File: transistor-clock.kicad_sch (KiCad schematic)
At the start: 41 parts, among them J1 Screw_Terminal_01x02, Q1 MMBT3904, Q2 MMBT3904, Q3 MMBT3904, Q4 DMP3099L, Q5 2N7002, Q6 MMBT3904, Q7 MMBT3904, Q8 MMBT3904, T1 Transformer_1P_SS

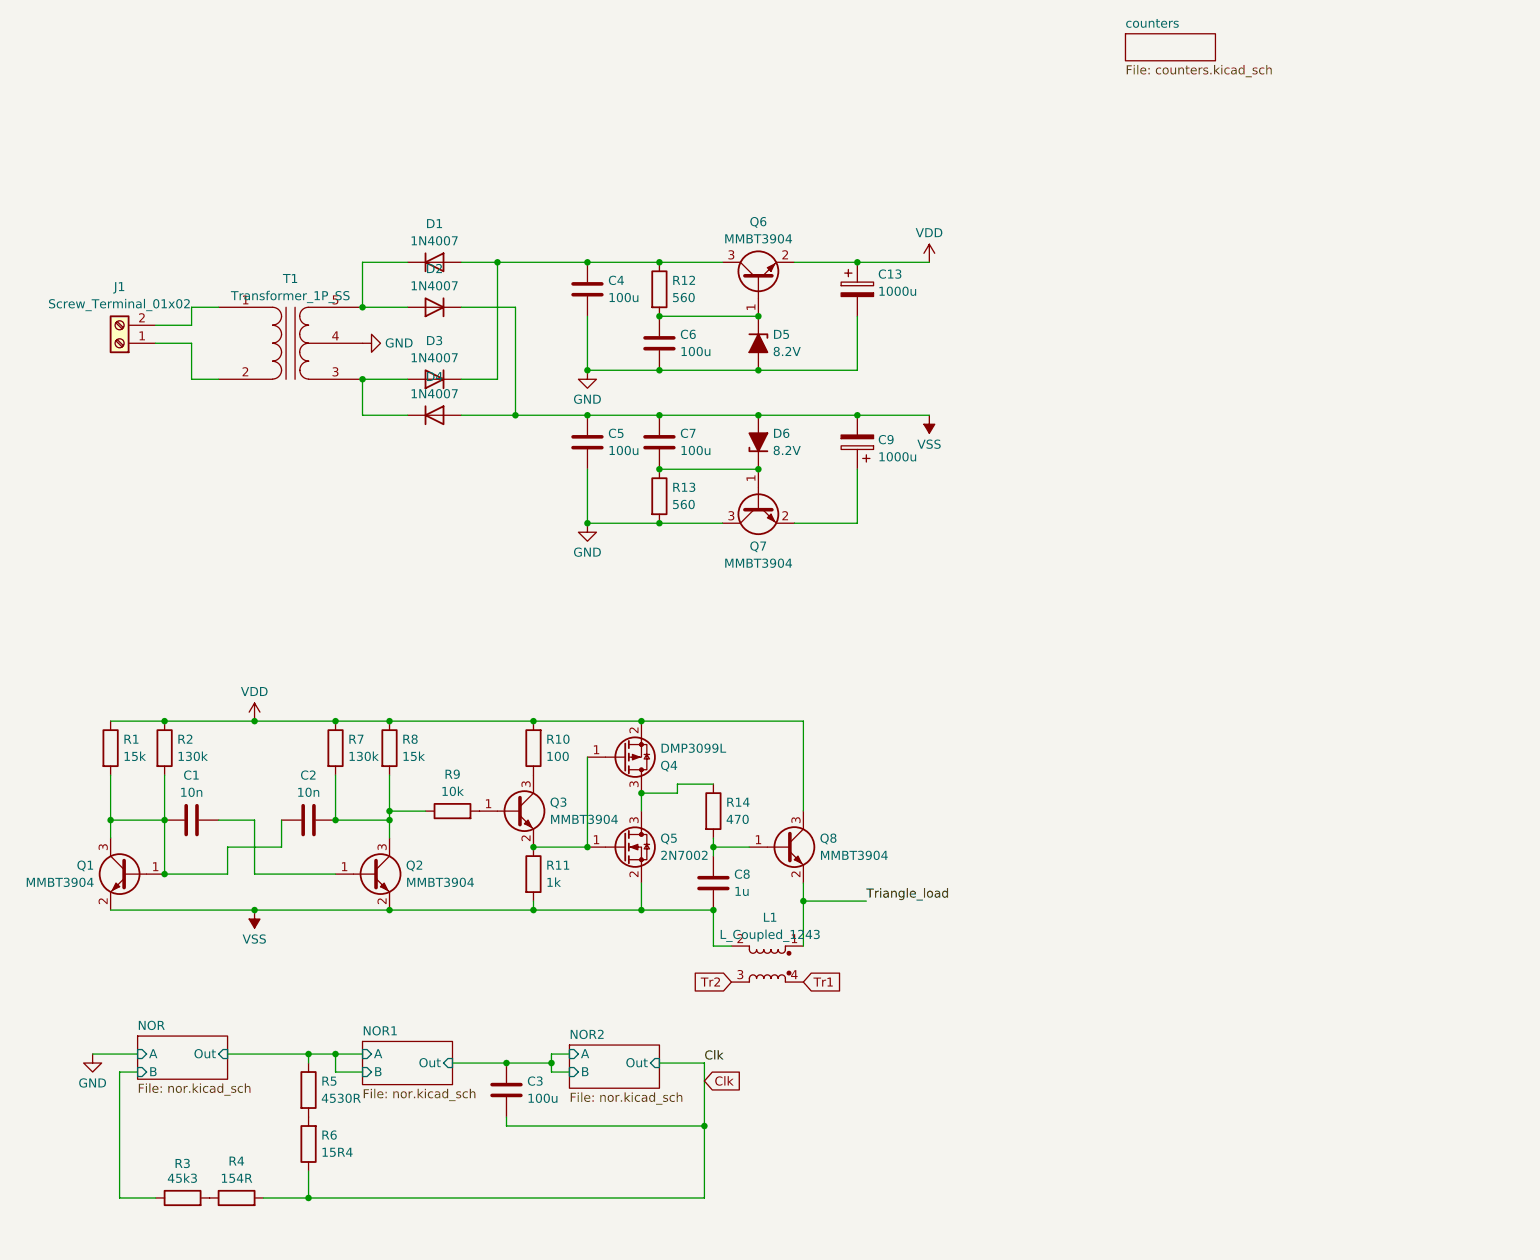
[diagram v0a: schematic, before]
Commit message: moved to 3v3
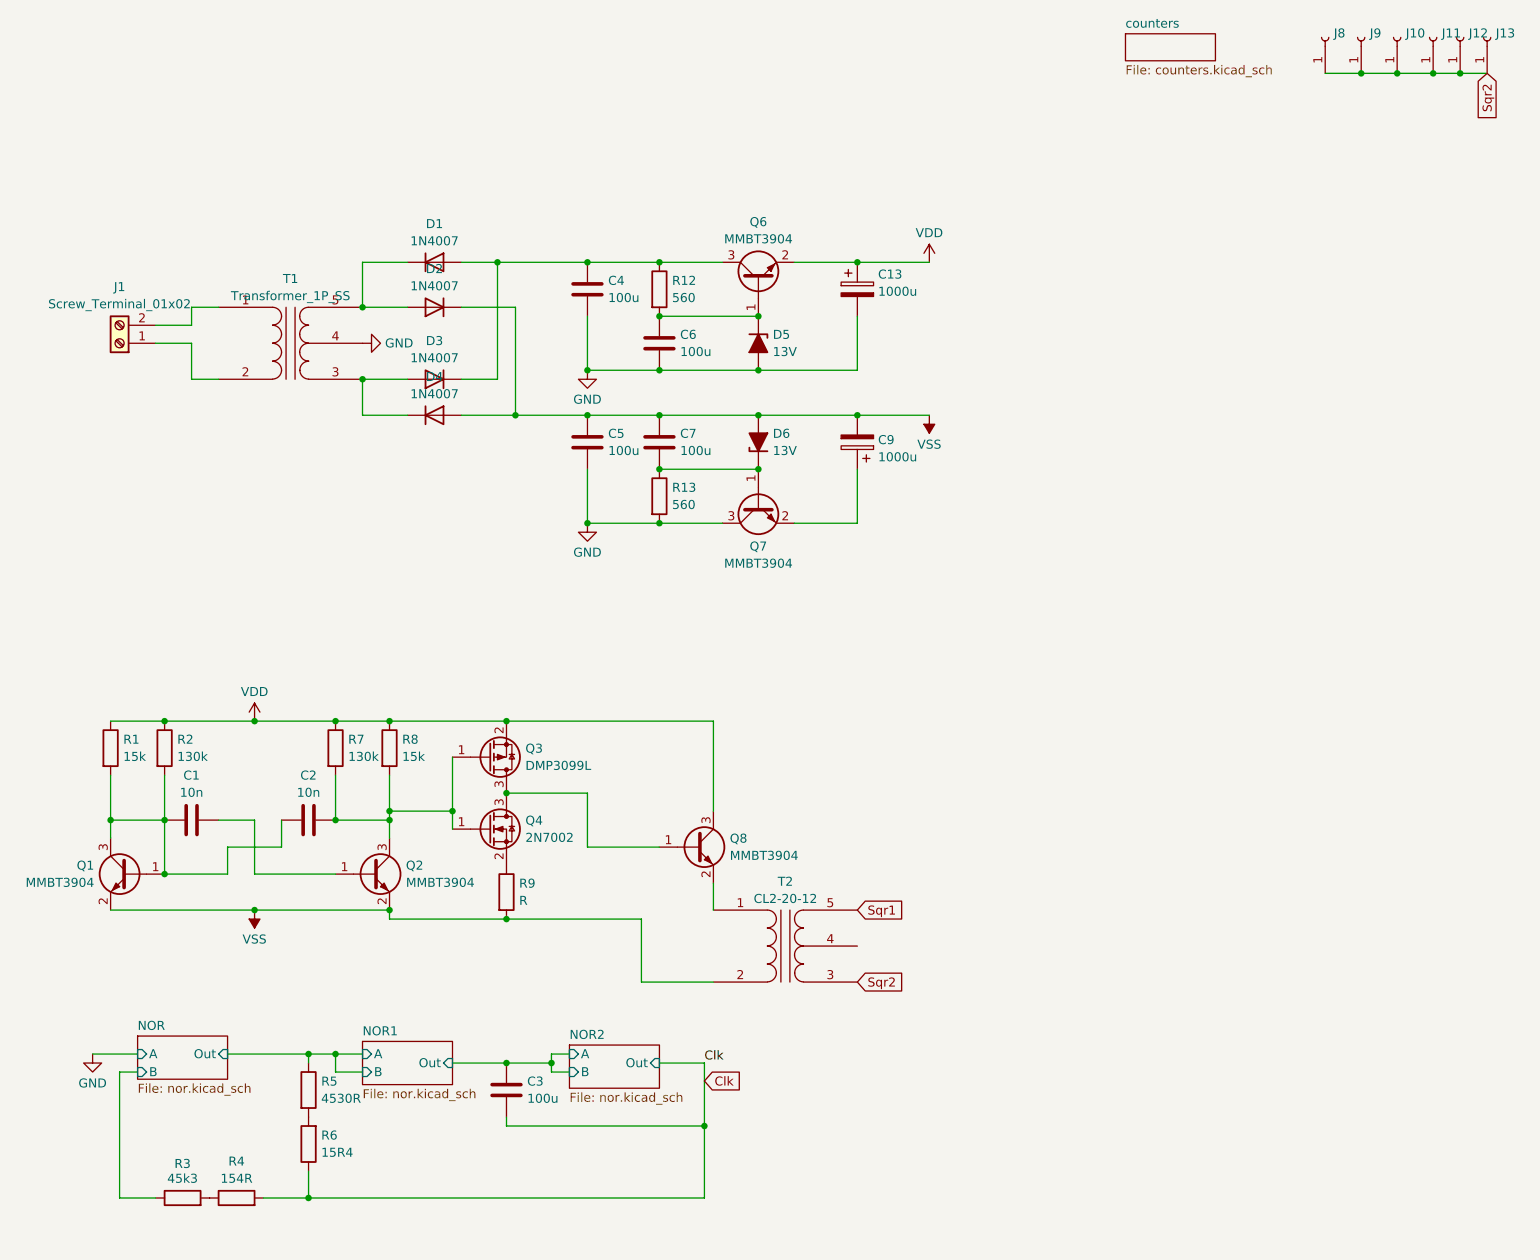
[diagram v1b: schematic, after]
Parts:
- removed C8: 1u, symbol Device:C
- removed L1: L_Coupled_1243, symbol Device:L_Coupled_1243
- removed Q3: MMBT3904, Package_TO_SOT_SMD:SOT-23, symbol Transistor_BJT:MMBT3904
- removed Q4: DMP3099L, Package_TO_SOT_SMD:SOT-23, symbol Transistor_FET:DMP3099L
- removed Q5: 2N7002, Package_TO_SOT_SMD:SOT-23, symbol Transistor_FET:2N7002
- removed R10: 100, Resistor_SMD:R_0402_1005Metric, symbol Device:R
- removed R11: 1k, Resistor_SMD:R_0402_1005Metric, symbol Device:R
- removed R14: 470, Resistor_SMD:R_0402_1005Metric, symbol Device:R
- added J10: m0_return, symbol Connector:Conn_01x01_Socket
- added J11: m1_return, symbol Connector:Conn_01x01_Socket
- added J12: h0_return, symbol Connector:Conn_01x01_Socket
- added J13: h1_return, symbol Connector:Conn_01x01_Socket
- added J8: s0_return, symbol Connector:Conn_01x01_Socket
- added J9: s1_return, symbol Connector:Conn_01x01_Socket
- added Q3: DMP3099L, Package_TO_SOT_SMD:SOT-23, symbol Transistor_FET:DMP3099L
- added Q4: 2N7002, Package_TO_SOT_SMD:SOT-23, symbol Transistor_FET:2N7002
- added T2: CL2-20-12, symbol Device:Transformer_1P_SS
- D5, D6: value 8.2V -> 13V
- R9: value 10k -> R; footprint Resistor_SMD:R_0402_1005Metric -> (none)
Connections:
- net VDD: now also Q3.2 (S)
- net VSS: now also R9.2, T2.2 (AB)
- net at C2.2, Q2.3 (C), R7.2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: now also Q3.1 (G), Q4.1 (G); no longer R9.1
- net at Q8.1 (B): now also Q3.3 (D), Q4.3 (D)
- net Triangle_load: no longer names the net of Q8.2 (E)
- net Triangle_load: now also T2.1 (AA)
- new net: Q4.2 (S), R9.1
- new net Sqr1: T2.5 (SB)
- new net Sqr2: J10.1 (Pin_1), J11.1 (Pin_1), J12.1 (Pin_1), J13.1 (Pin_1), J8.1 (Pin_1), J9.1 (Pin_1), T2.3 (SA)
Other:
- moved on the sheet: Q8

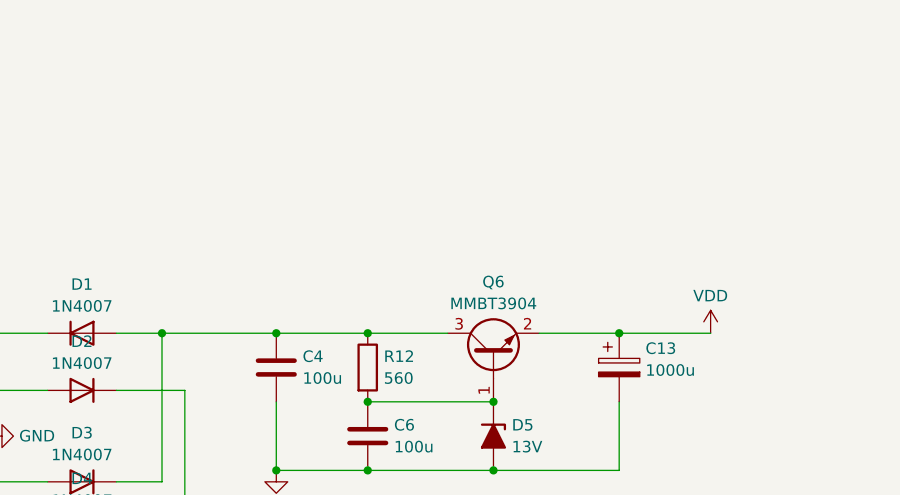
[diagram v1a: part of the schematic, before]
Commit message: added decoupling caps
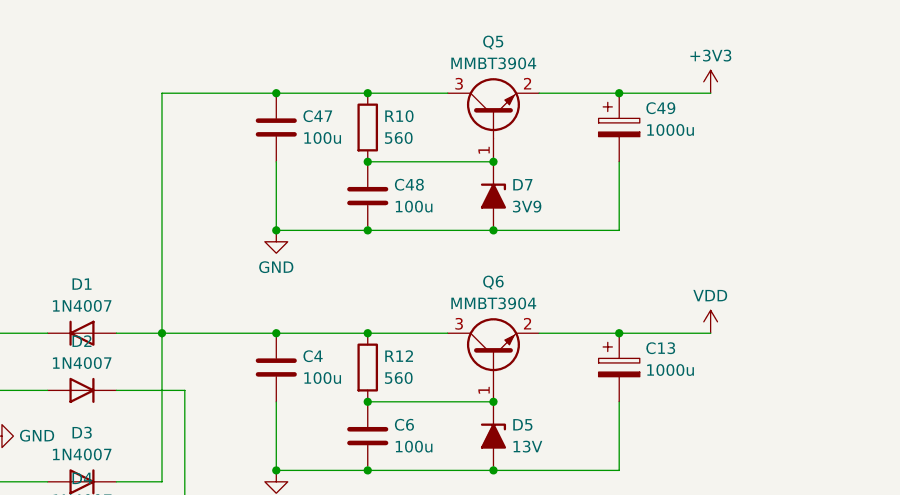
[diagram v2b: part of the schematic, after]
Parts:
- added C47, C48: 100u, symbol Device:C
- added C49: 1000u, symbol Device:C_Polarized
- added D7: 3V9, symbol Device:D_Zener_Filled
- added Q5: MMBT3904, Package_TO_SOT_SMD:SOT-23, symbol Transistor_BJT:MMBT3904
- added R10: 560, Resistor_SMD:R_0402_1005Metric, symbol Device:R
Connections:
- net GND: now also C47.2, C48.1, C49.2, D7.2 (A)
- net at C4.1, D1.2 (A), D3.1 (K)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: now also C47.1, Q5.3 (C), R10.1
- new net: C48.2, D7.1 (K), Q5.1 (B), R10.2
- new net +3V3: C49.1, Q5.2 (E)

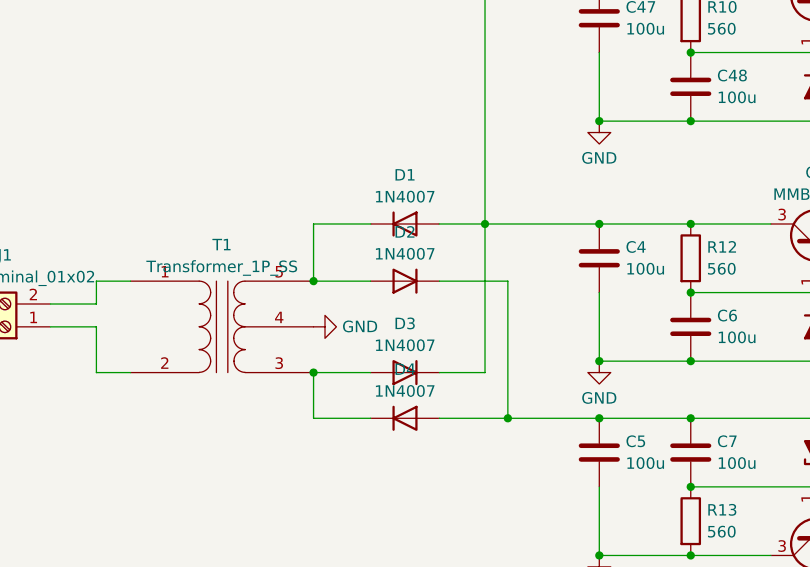
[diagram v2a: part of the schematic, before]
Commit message: changed rectifier diodes
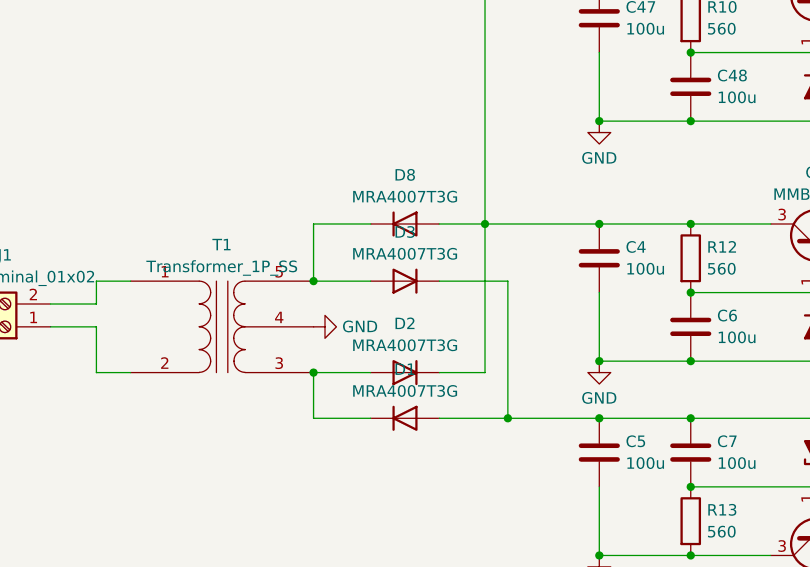
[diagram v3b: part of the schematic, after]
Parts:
- removed D1, D2, D3, D4: 1N4007, Diode_THT:D_DO-41_SOD81_P10.16mm_Horizontal, symbol Diode:1N4007
- added D1, D2, D3, D8: MRA4007T3G, Diode_SMD:D_SMA, symbol Diode:MRA4007T3G
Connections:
- net VSS: now also D1.2 (A), D3.1 (K)
- net at T1.5 (SB): now also D3.2 (A), D8.1 (K)
- net at T1.3 (SA): now also D1.1 (K), D2.2 (A)
- net at C4.1, C47.1, Q5.3 (C)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: now also D2.1 (K), D8.2 (A)
